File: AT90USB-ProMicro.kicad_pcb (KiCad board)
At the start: 2 copper layers, 18 x 33 mm, 17 parts, among them J1 Conn_01x12, J2 Conn_01x12, U1 AT90USB162-16MU, U2 MCP1703A-3302_SOT23, X1 ECS-2520MV-xxx-xx

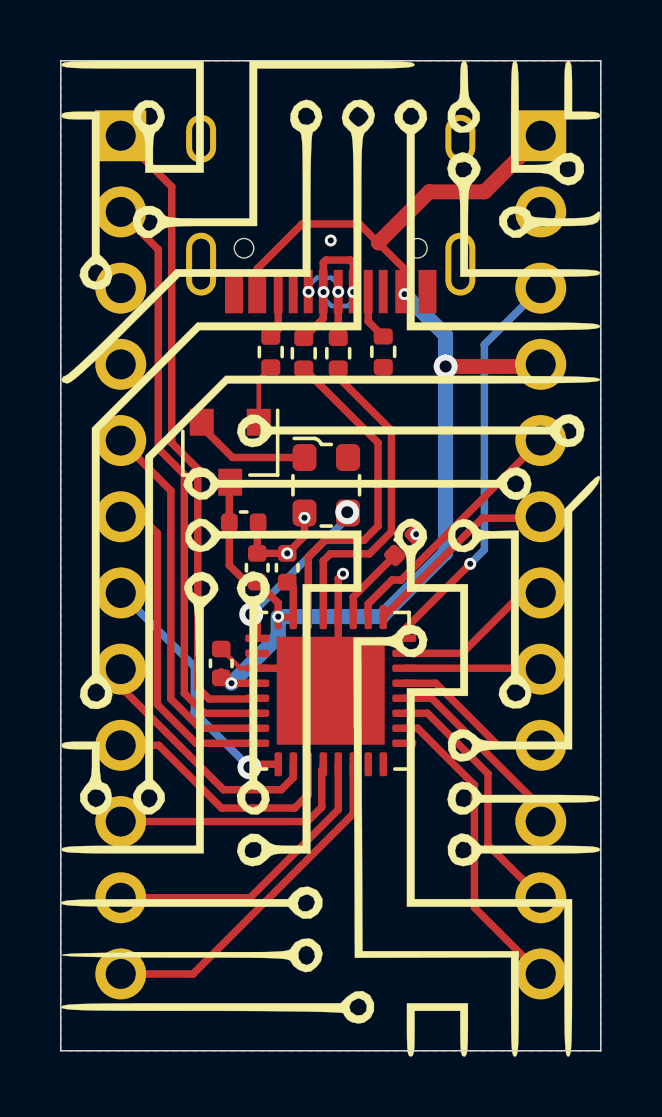
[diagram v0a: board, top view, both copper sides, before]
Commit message: updated readme + aded image
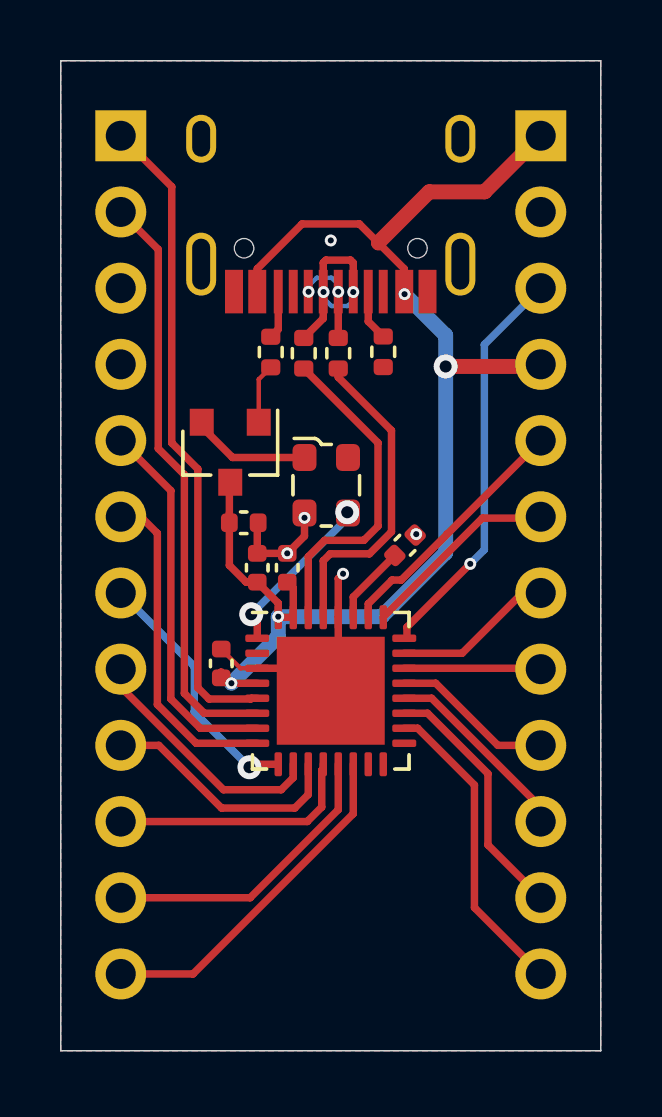
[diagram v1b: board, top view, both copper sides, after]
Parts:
- removed G*** (x2): LOGO, extra:patern

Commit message: Corrected alignment to match the  pro micro properly.
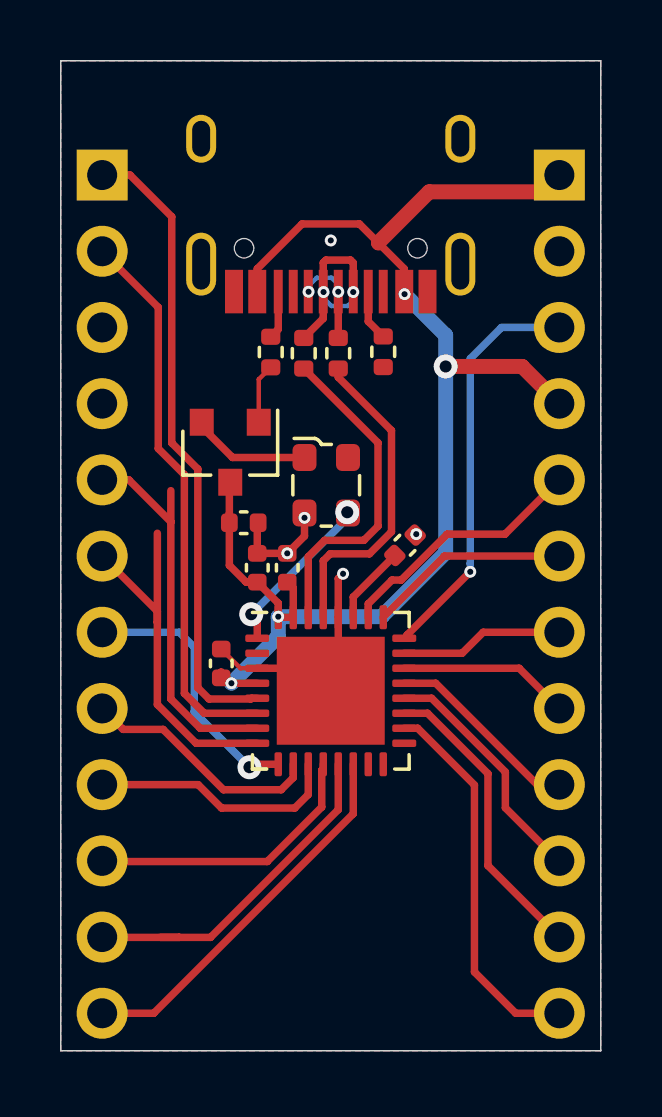
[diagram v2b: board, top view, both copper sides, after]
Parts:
- moved J1 1.45 mm to (124.4, 64.8)
- moved J2 1.45 mm to (139.6, 64.8)
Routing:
- net PB4: track 10.3 -> 12.8 mm
- net PD7: track 9.98 -> 11.8 mm
- net PB6: track 6.53 -> 8.12 mm
- net PB5: track 8.49 -> 10.1 mm
- net PD2: track 11.0 -> 12.5 mm
- net PD6: track 8.35 -> 9.53 mm
- net VBUS: track 45.1 -> 46.3 mm
- net PC7: track 4.56 -> 5.73 mm
- net PB7: track 5.41 -> 6.57 mm
- net PB0: track 11.6 -> 12.8 mm
- net PD0: track 19.6 -> 18.6 mm
- net PC5: track 6.64 -> 7.40 mm
- net PC2: track 21.6 -> 21.1 mm
- net PD1: track 12.6 -> 13.1 mm

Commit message: broke out spare MCU pins to a header.
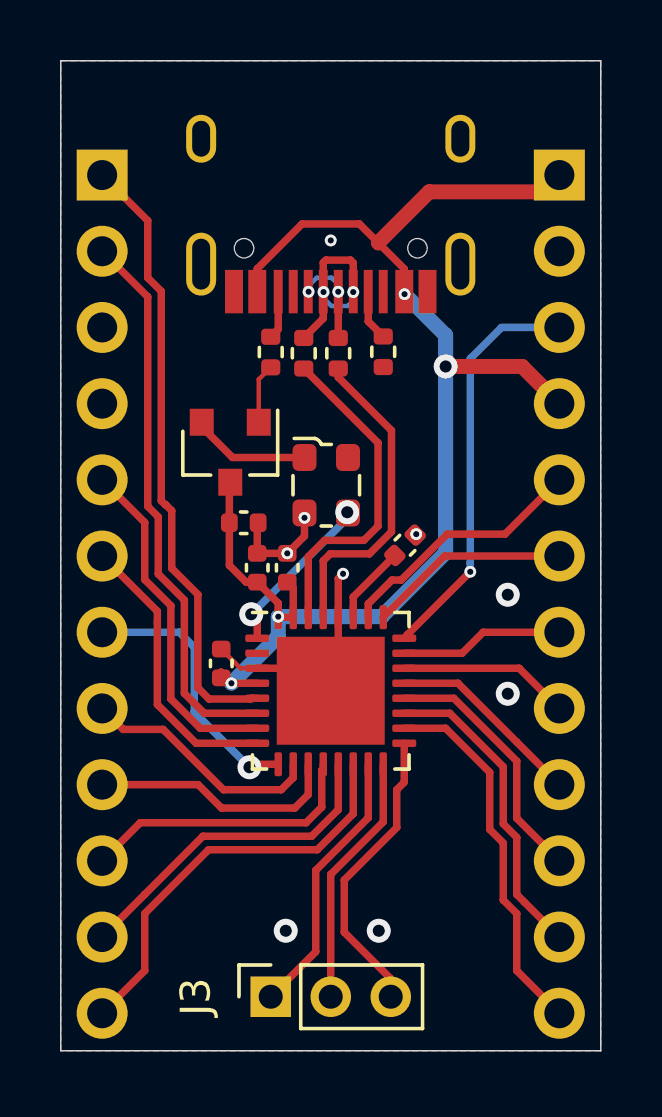
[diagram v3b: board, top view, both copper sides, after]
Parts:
- added J3: Conn_01x03, Connector_PinSocket_2.00mm:PinSocket_1x03_P2.00mm_Vertical, F.Cu at (130.0, 92.2)
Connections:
- U1 pad 15: (no net) -> PB1
- U1 pad 16: (no net) -> PB2
- U1 pad 17: (no net) -> PB3
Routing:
- net PB3: track 0.00 -> 9.92 mm
- net PB1: track 0.00 -> 9.10 mm
- net PB2: track 0.00 -> 8.47 mm
- net PD2: track 12.5 -> 9.58 mm
- net PD1: track 13.1 -> 11.5 mm
- net PB0: track 12.8 -> 13.9 mm
- net PD7: track 11.8 -> 11.2 mm
- net PC2: track 21.1 -> 20.6 mm
- net GND: vias 5 -> 9

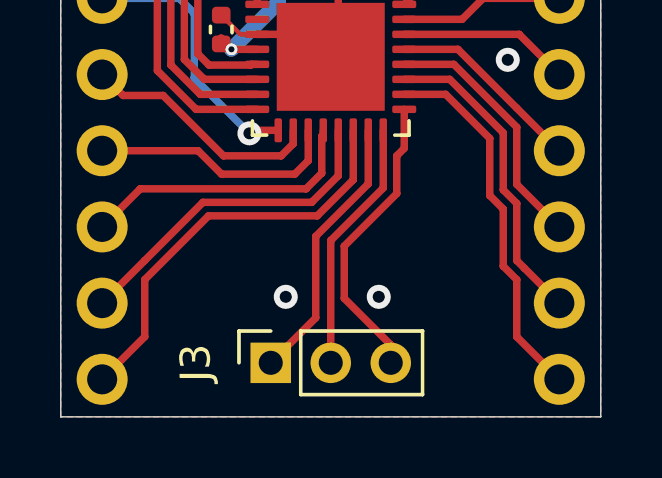
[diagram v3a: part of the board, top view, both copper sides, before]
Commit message: swapped header to be correct way. may need to re-align it to fit other pro-micro like boards.
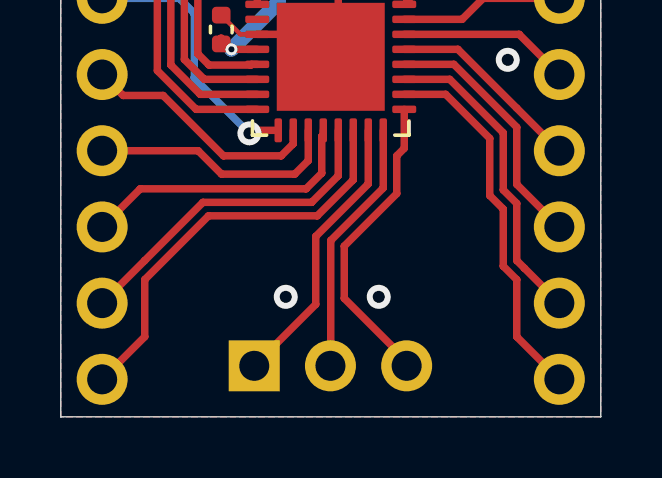
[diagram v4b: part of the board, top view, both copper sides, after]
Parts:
- J3: footprint Connector_PinSocket_2.00mm:PinSocket_1x03_P2.00mm_Vertical -> Connector_PinHeader_2.54mm:PinHeader_1x03_P2.54mm_Vertical; moved to B.Cu
- moved J3 0.56 mm to (129.4, 92.3), turned to 270 degrees

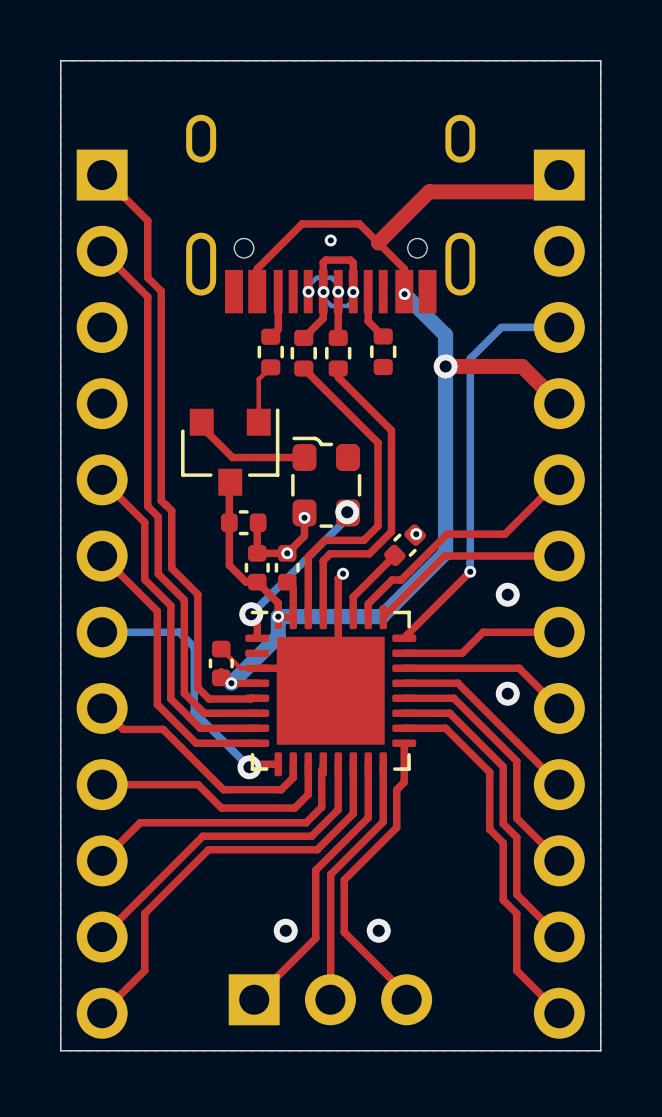
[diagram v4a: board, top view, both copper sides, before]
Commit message: Added some silkscreen notes and realigned some capacitors, resistors and usb traces
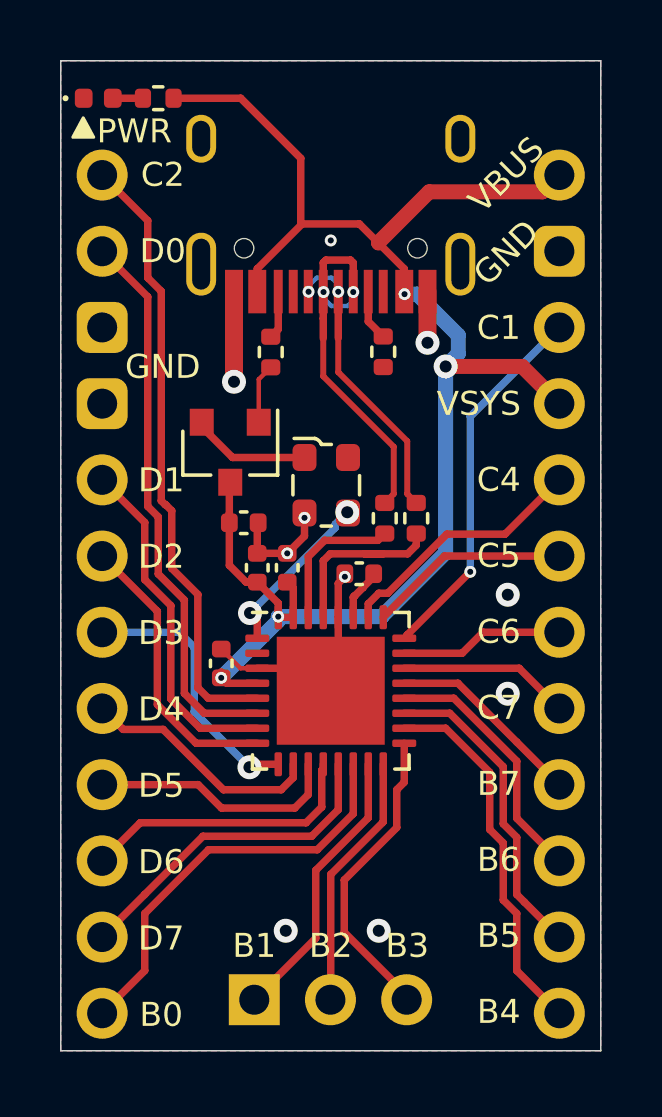
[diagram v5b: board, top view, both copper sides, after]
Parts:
- added D1: 0402 LED, LED_SMD:LED_0402_1005Metric, F.Cu at (124.2, 62.2)
- added R5: 2.2K 0402, Resistor_SMD:R_0402_1005Metric, F.Cu at (126.2, 62.2)
- moved R4 6.13 mm to (133.8, 76.2)
- moved R3 6.08 mm to (134.8, 76.2)
- moved C2 1.80 mm to (132.9, 78.1), turned to 180 degrees
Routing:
- net VBUS: track 46.3 -> 54.2 mm
- net USB_D+: track 3.19 -> 9.76 mm
- net USB_D-: track 6.47 -> 12.8 mm
- net Net-(R4-Pad1): track 11.0 -> 4.89 mm
- net GND: track 13.9 -> 18.5 mm, vias 9 -> 10
- net Net-(R3-Pad1): track 10.7 -> 6.19 mm
- net PC1: track 13.6 -> 12.4 mm
- net Net-(D1-Pad2): track 0.00 -> 1.00 mm
- net Net-(C2-Pad1): track 2.63 -> 1.64 mm
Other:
- board text added: "B0"
- board text added: "B1"
- board text added: "B2"
- board text added: "B3"
- board text added: "B4"
- board text added: "B5"
- board text added: "B6"
- board text added: "B7"
- board text added: "C1"
- board text added: "C2"
- board text added: "C4"
- board text added: "C5"
- board text added: "C6"
- board text added: "C7"
- board text added: "D0"
- board text added: "D1"
- board text added: "D2"
- board text added: "D3"
- board text added: "D4"
- board text added: "D5"
- board text added: "D6"
- board text added: "D7"
- board text added: "GND"
- board text added: "PWR"
- board text added: "VBUS"
- board text added: "VSYS"

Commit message: added a couple more decoupling capacitors, one for 3.3V LDO and one for the clock
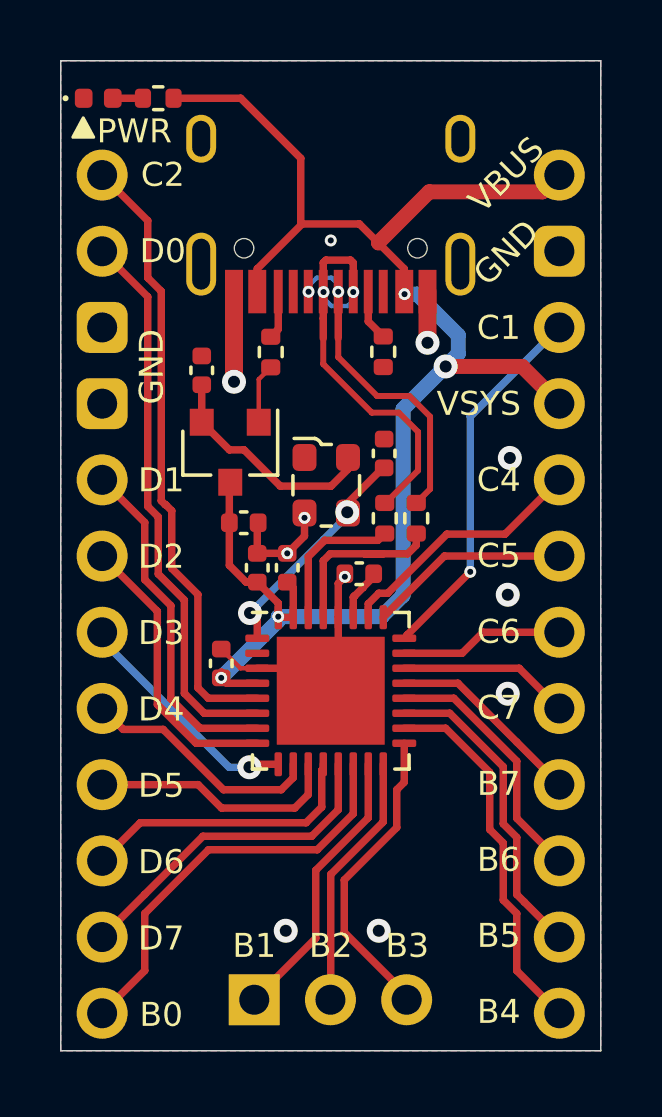
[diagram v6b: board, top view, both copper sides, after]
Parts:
- added C6: 0.1uf 0402, Capacitor_SMD:C_0402_1005Metric, F.Cu at (127.7, 71.3)
- added C7: 15pF 0402, Capacitor_SMD:C_0402_1005Metric, F.Cu at (133.8, 74.1)
- X1: value ECS-2520MV-xxx-xx -> O925208MEDA4SI
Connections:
- U2 pad 2: Net-(U2-Pad2) -> Net-(C6-Pad2)
- X1 pad 1: Net-(U2-Pad2) -> (no net)
- X1 pad 4: (no net) -> Net-(C6-Pad2)
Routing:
- net Net-(C6-Pad2): track 0.00 -> 7.78 mm
- net Net-(U2-Pad2): track 4.00 -> 0.00 mm
- net XTAL1: track 5.64 -> 7.66 mm
- net USB_D-: track 12.8 -> 14.0 mm
- net PD3: track 9.11 -> 8.00 mm
- net USB_D+: track 9.76 -> 10.8 mm
- net GND: vias 10 -> 11

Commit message: changed part description in schematic
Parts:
- added Ref**: Val**, MechboardsLogo:mechboardsLOGO_5mm, F.Cu at (132.0, 87.1)

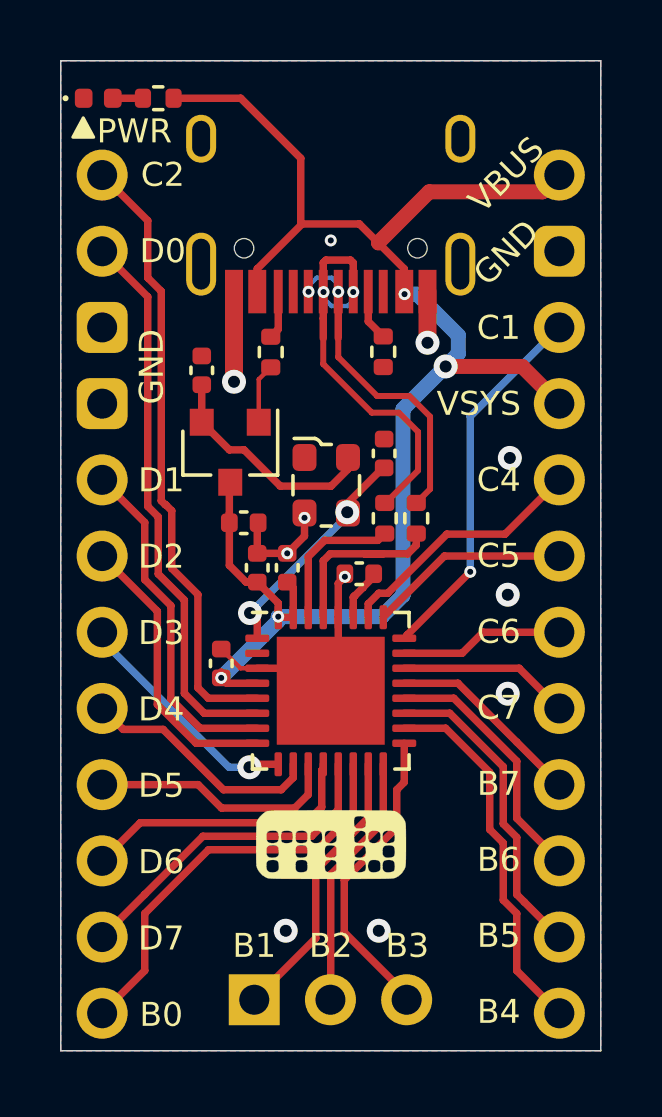
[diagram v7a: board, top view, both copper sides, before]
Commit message: Corrected errors as per DRC
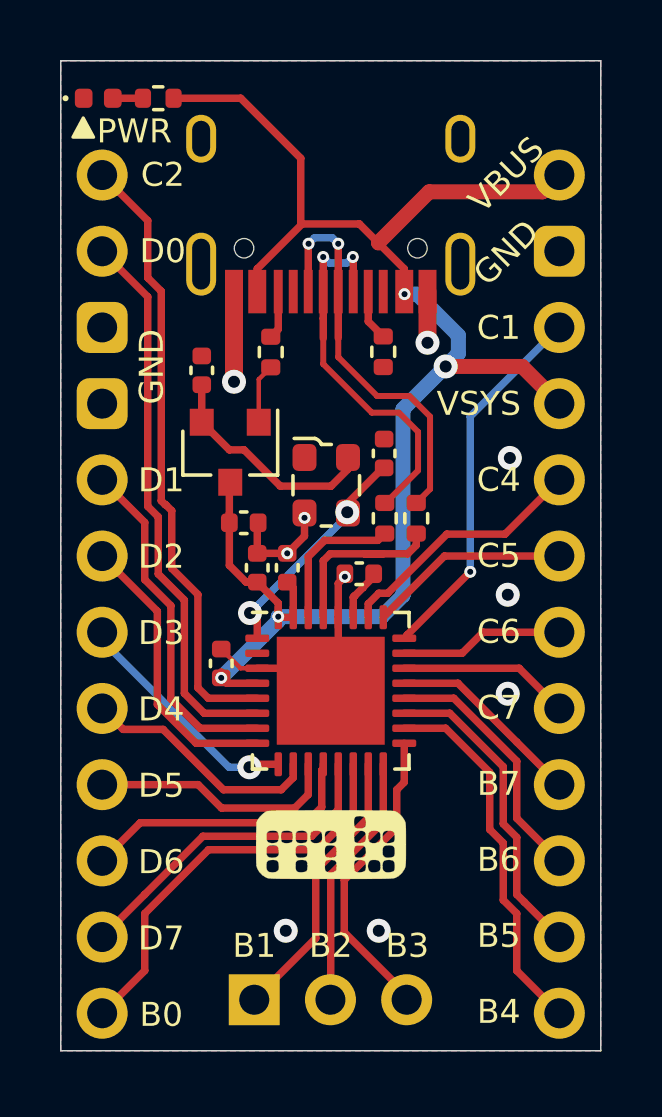
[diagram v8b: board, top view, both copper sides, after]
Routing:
- net USB_D+: track 10.8 -> 13.5 mm
- net USB_D-: track 14.0 -> 12.8 mm
- net GND: vias 11 -> 10
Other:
- net class Default: clearance 0.2 -> 0.127
- rule trace_clearance: 0.2 -> 0.127
- rule trace_min: 0.126 -> 0.127
